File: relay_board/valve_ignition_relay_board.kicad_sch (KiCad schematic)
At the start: 19 parts, among them J1 Programming Header, J5 CAN Connector Left, J6 CAN Connector Right, U10 INA180, U11 INA180, Y1 12 MHz

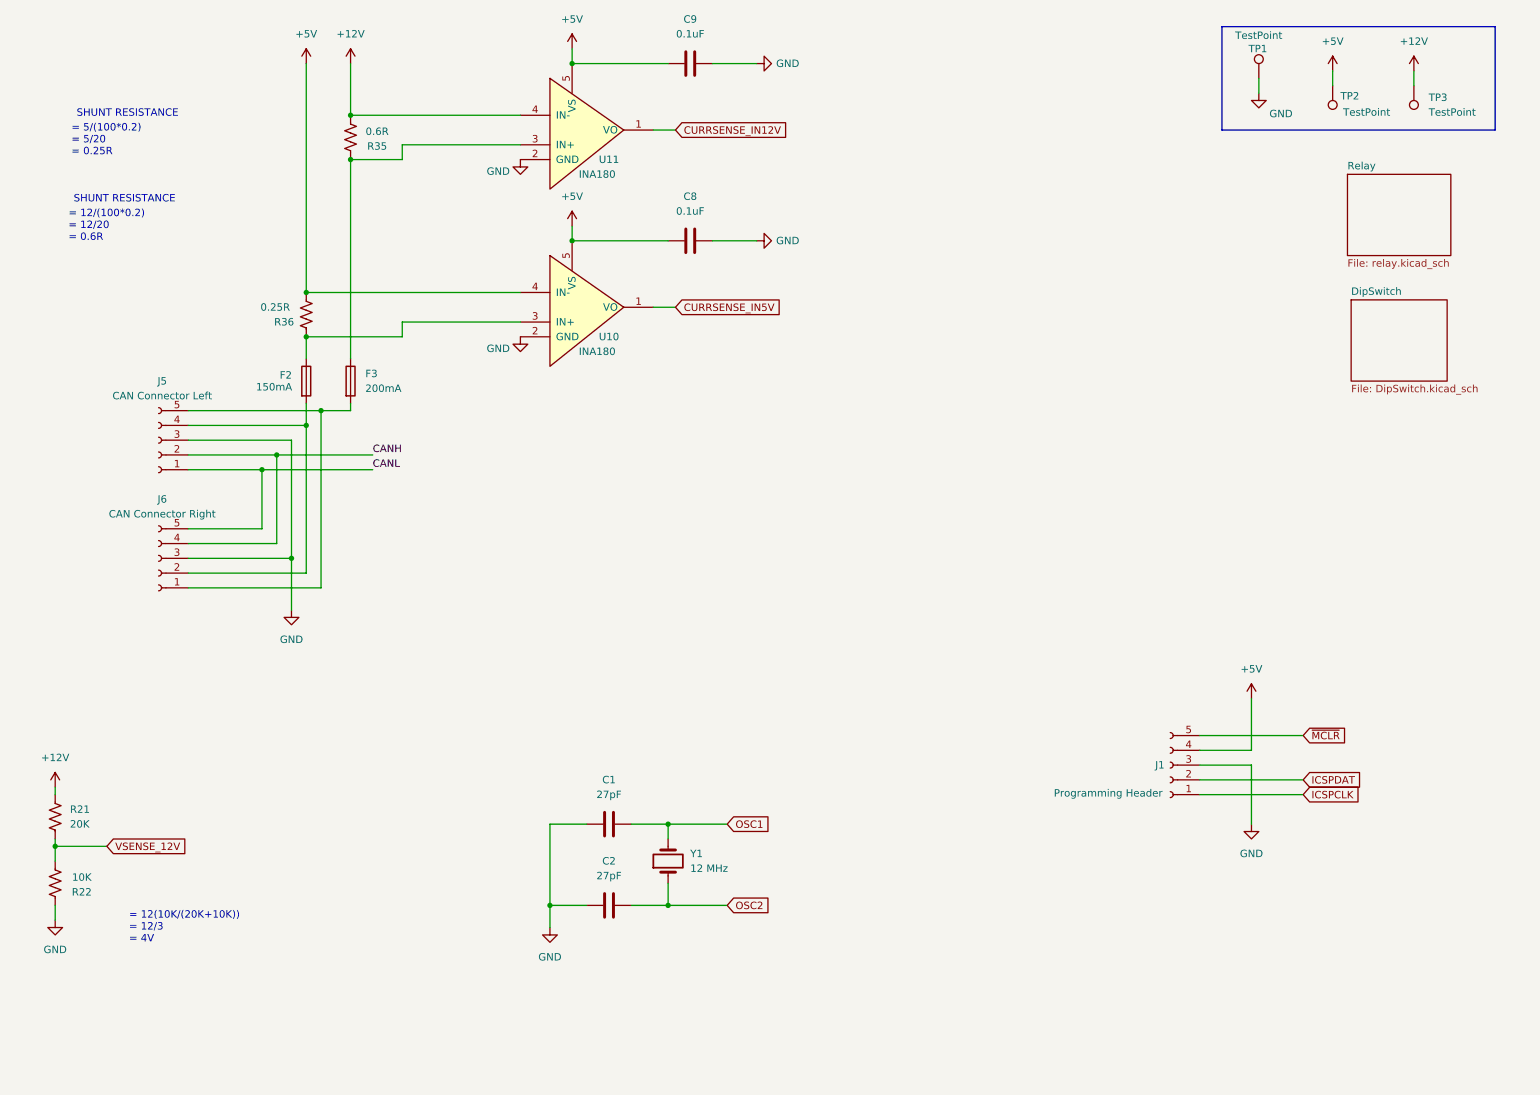
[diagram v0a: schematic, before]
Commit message: Changed to Hierarchical labels and added reverse voltage protection. Still need to do resistor math for voltage protection.
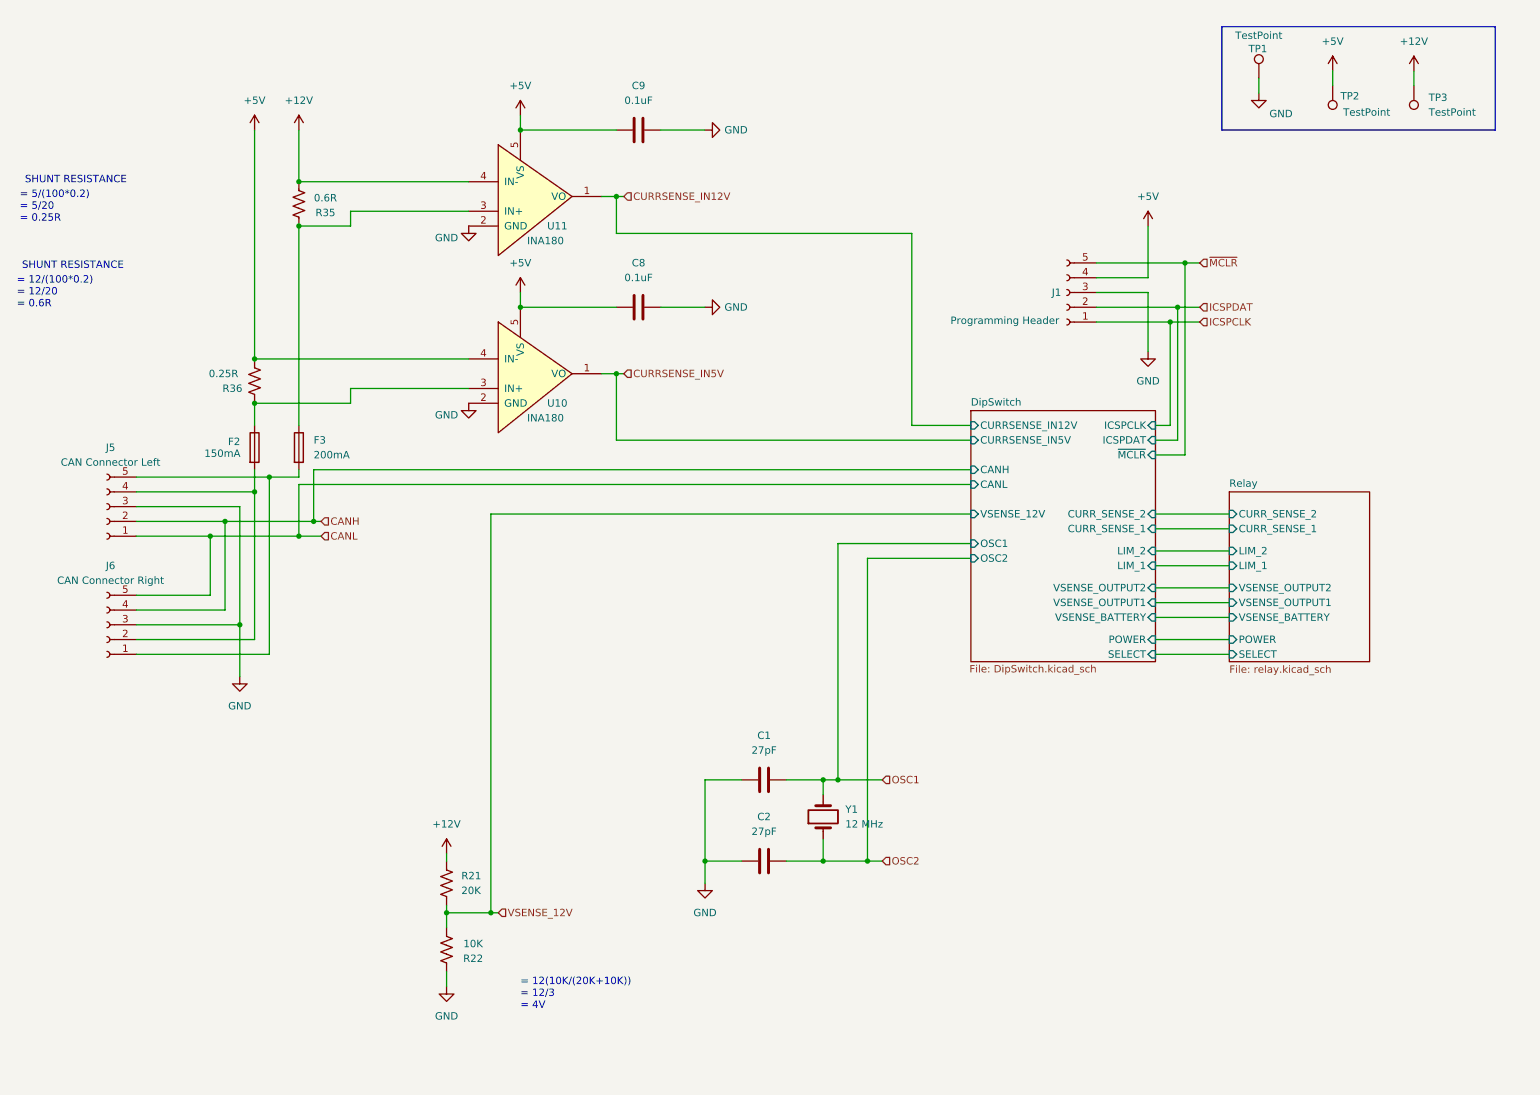
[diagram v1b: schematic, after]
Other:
- sheet DipSwitch ports: added CANH, CANL, CURRSENSE_IN12V, CURRSENSE_IN5V, CURR_SENSE_1, CURR_SENSE_2, ICSPCLK, ICSPDAT, LIM_1, LIM_2, OSC1, OSC2, POWER, SELECT, VSENSE_12V, VSENSE_BATTERY, VSENSE_OUTPUT1, VSENSE_OUTPUT2, ~{MCLR}; removed none
- sheet Relay ports: added CURR_SENSE_1, CURR_SENSE_2, LIM_1, LIM_2, POWER, SELECT, VSENSE_BATTERY, VSENSE_OUTPUT1, VSENSE_OUTPUT2; removed none
- moved on the sheet: C1, C2, C8, C9, F2, F3, J1, J5, J6, R21, R22, R35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

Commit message: requested changes 1
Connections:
- net CANH renamed DipSwitch/CANH
- net CANL renamed DipSwitch/CANL
- net CURRSENSE_IN12V renamed DipSwitch/CURRSENSE_IN12V
- net CURRSENSE_IN5V renamed DipSwitch/CURRSENSE_IN5V
- net ICSPCLK renamed DipSwitch/ICSPCLK
- net ICSPDAT renamed DipSwitch/ICSPDAT
- net OSC1 renamed DipSwitch/OSC1
- net OSC2 renamed DipSwitch/OSC2
- net VSENSE_12V renamed DipSwitch/VSENSE_12V
- net ~{MCLR} renamed DipSwitch/~{MCLR}

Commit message: fix symbols; routing v1
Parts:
- removed R21: 20K, Resistor_SMD:R_0805_2012Metric_Pad1.20x1.40mm_HandSolder, symbol Device:R_US
- removed R22: 10K, Resistor_SMD:R_0805_2012Metric_Pad1.20x1.40mm_HandSolder, symbol Device:R_US
- removed R36: 0.25R, Resistor_SMD:R_0805_2012Metric_Pad1.20x1.40mm_HandSolder, symbol Device:R_US
- added H1, H2, H3, H4: MountingHole, MountingHole:MountingHole_3.2mm_M3, symbol Mechanical:MountingHole
- added R29: 0.25, Resistor_SMD:R_0805_2012Metric_Pad1.20x1.40mm_HandSolder, symbol Device:R_US
- J1: footprint Connector_JST:JST_XH_S5B-XH-A-1_1x05_P2.50mm_Horizontal -> canhw_footprints:PinSocket_5x2.54_SMD_90deg_952-3198-1-ND
- TP1, TP2, TP3: now left out of the parts list
- U10, U11: value INA180 -> INA180A3
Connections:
- net +5V: now also J1.2 (Pin_2), R29.2; no longer J1.4 (Pin_4)
- net DipSwitch/ICSPCLK: now also J1.5 (Pin_5); no longer J1.1 (Pin_1)
- net DipSwitch/ICSPDAT: now also J1.4 (Pin_4); no longer J1.2 (Pin_2)
- net DipSwitch/~{MCLR}: now also J1.1 (Pin_1); no longer J1.5 (Pin_5)
- net at F2.1, U10.3 (IN+): now also R29.1
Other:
- sheet DipSwitch ports: added none; removed VSENSE_12V
- note removed: "= 12(10K/(20K+10K)) = 12/3 = 4V"
- moved on the sheet: C1, C2, C8, C9, F2, F3, J1, J5, J6, R35, Y1

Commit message: lowpass current sense; move power traces to FCu
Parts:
- added C12, C13: 1.6nF, Capacitor_SMD:C_0805_2012Metric_Pad1.18x1.45mm_HandSolder, symbol Device:C
- added R32, R33: 500R, Resistor_SMD:R_0805_2012Metric_Pad1.20x1.40mm_HandSolder, symbol Device:R_US
- R29: value 0.25 -> 0.25R
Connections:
- net DipSwitch/CURRSENSE_IN12V: now also C12.2, R32.1; no longer U11.1 (VO)
- net DipSwitch/CURRSENSE_IN5V: now also C13.2, R33.1; no longer U10.1 (VO)
- net GND: now also C12.1, C13.1
- new net: R32.2, U11.1 (VO)
- new net: R33.2, U10.1 (VO)
